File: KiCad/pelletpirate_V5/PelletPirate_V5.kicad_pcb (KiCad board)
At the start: 2 copper layers, 65 x 110 mm, 105 parts, among them J1 SJ1-3523NG_Jack_PP, J2 SJ1-3523NG_Jack_PP, J3 SJ1-3523NG_Jack_PP, J4 SJ1-3523NG_Jack_PP, J5 SJ1-3523NG_Jack_PP, J6 Conn_01x04, T1 BTA12-Triac, T2 BTA12-Triac, T3 BTA12-Triac

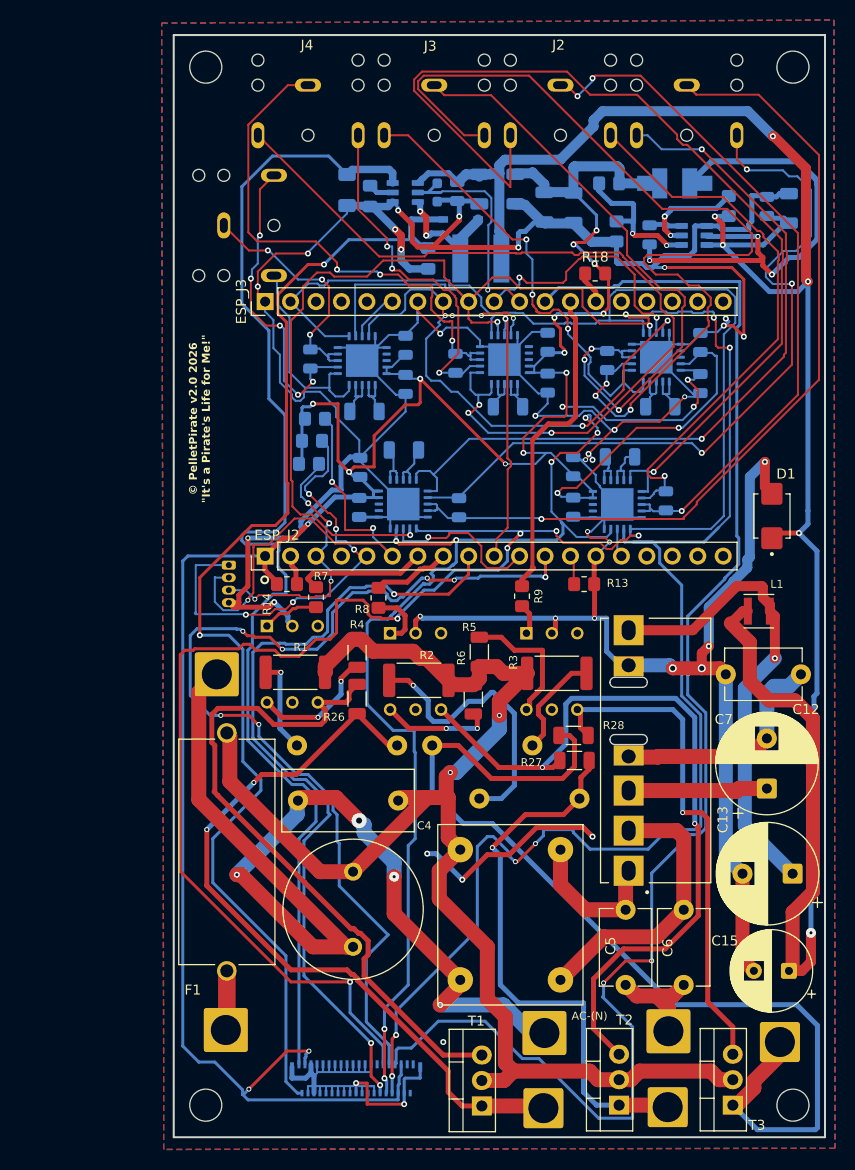
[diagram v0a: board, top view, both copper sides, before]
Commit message: V5 Phase B/C checkpoint: Update-PCB applied, placement in progress
Board now carries the full V5 netlist: S3/USB/ZC/hopper/switch/LED
footprints on board, SDO net renamed to ALL_SDO across existing copper
(tracks preserved), fan channel = MOC3053M with verified Panasonic
ERJ-UP6F1800V drive resistors, DNP flags cleared, WirePad5 relinked.
New parts rough-placed; nets locked next, then arrangement and routing.
FPC1 decision: moving to top-left (side B) pending flex-reach check.

Hard-won process lessons this session: Update-PCB must run with
re-link-by-reference CHECKED (UUID matching deletes re-associated
footprints); preview dialogs can serve stale reports — regenerate
fresh after schematic saves; editor memory can diverge from disk after
undo chains — verify against the file and close-without-save to recover.

Co-Authored-By: Claude Fable 5 <noreply@anthropic.com>
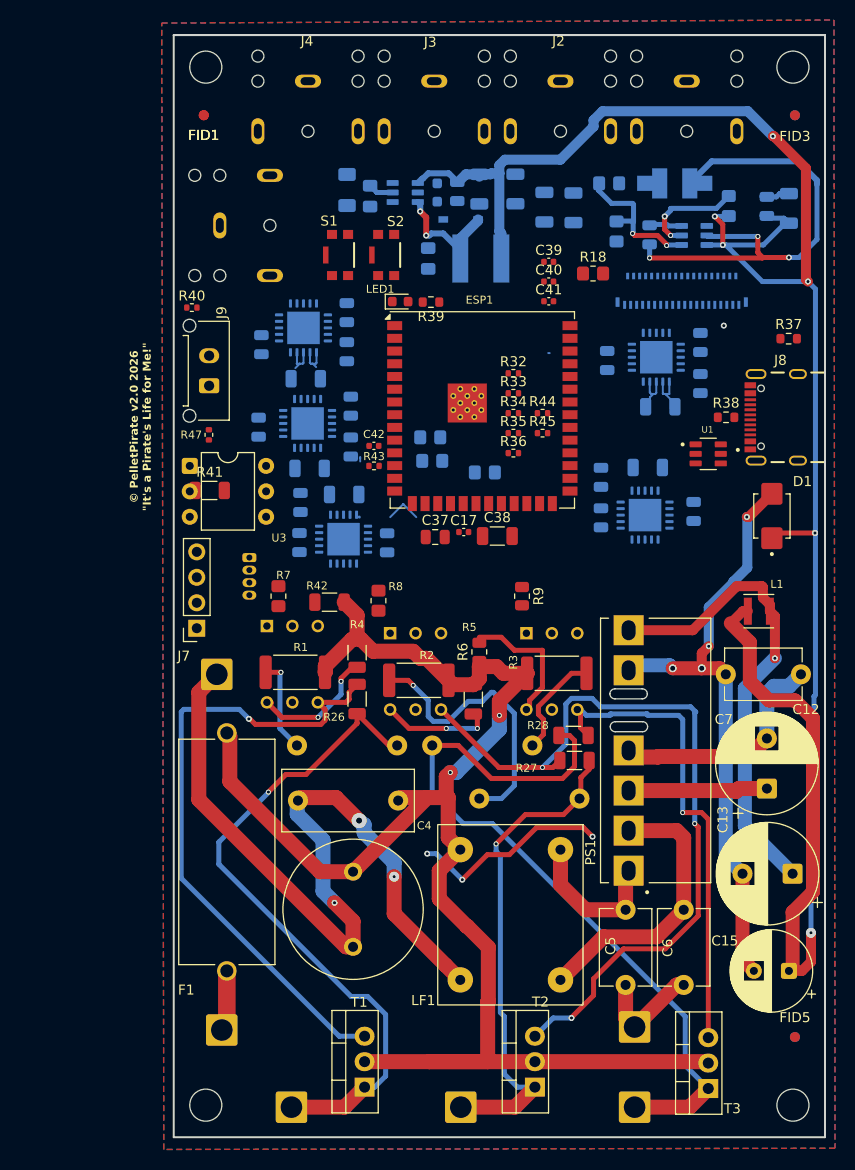
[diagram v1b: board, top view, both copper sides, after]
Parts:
- removed AC-(N): AC-NEUTRAL, Connector_Wire:SolderWire-2.5sqmm_1x01_D2.4mm_OD4.4mm
- removed ESP_J2: PelletPirate_J2_01toJ2_19, ESP32-Footprint-PelletPirate-02x19x2=39:PinHeader_J2x19_P2.54mm_Vertical_PelletPirate
- removed ESP_J3: PelletPirate_J3_01toJ3_19, ESP32-Footprint-PelletPirate-02x19x2=39:PinHeader_J3x19_P2.54mm_Vertical_PelletPirate
- removed R13, R14: 10KΩ, Resistor_SMD:R_0805_2012Metric_Pad1.20x1.40mm_HandSolder
- added C17: 0.1µF 25V, Capacitor_SMD:C_0402_1005Metric, F.Cu at (148.9, 89.6)
- added C37: 1µF 25V, Capacitor_SMD:C_0805_2012Metric, F.Cu at (146.1, 90.1)
- added C38: 10µF 25V, Capacitor_SMD:C_1206_3216Metric, F.Cu at (152.3, 90.0)
- added C39: 0.1µF 25V, Capacitor_SMD:C_0402_1005Metric, F.Cu at (157.4, 62.6)
- added C40: 0.1µF 25V, Capacitor_SMD:C_0402_1005Metric, F.Cu at (157.4, 64.6)
- added C41: 0.1µF 25V, Capacitor_SMD:C_0402_1005Metric, F.Cu at (157.4, 66.6)
- added C42: 1000pF 50V, Capacitor_SMD:C_0402_1005Metric, F.Cu at (140.0, 81.0)
- added ESP1: ESP32-S3-WROOM-1U-N16R8-flyman, Expressif_S3_N16R8_Chip_N1U:ESP32-S3-WROOM-1U-flyman, F.Cu at (150.8, 77.4)
- added FID1 (x2): Fiducial_1mm_Mask2mm, Fiducial:Fiducial_1mm_Mask2mm, F.Cu at (123.0, 48.0)
- added FID3: Fiducial_1mm_Mask2mm, Fiducial:Fiducial_1mm_Mask2mm, F.Cu at (182.0, 48.0)
- added FID4: Fiducial_1mm_Mask2mm, Fiducial:Fiducial_1mm_Mask2mm, B.Cu at (182.0, 48.0)
- added FID5: Fiducial_1mm_Mask2mm, Fiducial:Fiducial_1mm_Mask2mm, F.Cu at (182.0, 140.0)
- added FID6: Fiducial_1mm_Mask2mm, Fiducial:Fiducial_1mm_Mask2mm, B.Cu at (182.0, 140.0)
- added J7: Conn_01x04_Socket, Connector_PinSocket_2.54mm:PinSocket_1x04_P2.54mm_Vertical, F.Cu at (122.3, 99.2)
- added J8: USB4105-GF-A_fly, USB_try2:GCT_USB4105-GF-A_flyman, F.Cu at (182.3, 78.2)
- added J9: Conn_01x02, Connector_Molex:Molex_Micro-Fit_3.0_43650-0215_1x02_P3.00mm_Vertical, F.Cu at (123.5, 75.0)
- added LED1: LTST-C191KGKT_flyman, LED_SMD:LED_0603_1608Metric, F.Cu at (142.6, 66.6)
- added R32: 10KΩ, Resistor_SMD:R_0402_1005Metric, F.Cu at (153.9, 73.8)
- added R33: 10KΩ, Resistor_SMD:R_0402_1005Metric, F.Cu at (153.9, 75.8)
- added R34: 10KΩ, Resistor_SMD:R_0402_1005Metric, F.Cu at (153.9, 77.7)
- added R35: 10KΩ, Resistor_SMD:R_0402_1005Metric, F.Cu at (153.9, 79.7)
- added R36: 10KΩ, Resistor_SMD:R_0402_1005Metric, F.Cu at (153.9, 81.7)
- added R37: 5.1KΩ, Resistor_SMD:R_0603_1608Metric, F.Cu at (181.4, 70.3)
- added R38: 5.1KΩ, Resistor_SMD:R_0603_1608Metric, F.Cu at (175.1, 78.2)
- added R39: 1KΩ, Resistor_SMD:R_0603_1608Metric, F.Cu at (145.7, 66.7)
- added R40: 10KΩ, Resistor_SMD:R_0402_1005Metric, F.Cu at (121.8, 67.2)
- added R41: 15KΩ, Resistor_SMD:R_1206_3216Metric, F.Cu at (123.6, 85.5)
- added R42: 15KΩ, Resistor_SMD:R_1206_3216Metric, F.Cu at (135.6, 96.6)
- added R43: 10KΩ, Resistor_SMD:R_0402_1005Metric, F.Cu at (140.0, 83.0)
- added R44: 10KΩ, Resistor_SMD:R_0402_1005Metric, F.Cu at (156.8, 77.7)
- added R45: 10KΩ, Resistor_SMD:R_0402_1005Metric, F.Cu at (156.8, 79.7)
- added R47: 100Ω, Resistor_SMD:R_0402_1005Metric, F.Cu at (123.5, 79.9)
- added S1: KMR221GLFS, KMR221GLFS_SMD_boot_reset_switch:SW_KMR221GLFS, F.Cu at (136.6, 62.0)
- added S2: KMR221GLFS, KMR221GLFS_SMD_boot_reset_switch:SW_KMR221GLFS, F.Cu at (141.2, 62.0)
- added U1: USBLC6-2SC6, USBC6-2SC6:SOT95P280X145-6N, F.Cu at (173.3, 81.8)
- added U3: H11AA1M, Package_DIP:DIP-6_W7.62mm, F.Cu at (121.6, 83.0)
- Earth1, WirePad1, WirePad2: footprint Connector_Wire:SolderWire-2.5sqmm_1x01_D2.4mm_OD4.4mm -> Connector_Wire:SolderWire-1.5sqmm_1x01_D1.7mm_OD3mm
- MOC3: value MOC3063M -> MOC3053M; footprint MOC3063M-PP2:MOC3063M-PP2 -> MOC3053M_Opto_FanPulse:DIP762W46P254L851H508Q6
- PS1: footprint PBO-5F-12_PP_Try2:PBO-5F-12_pp2 -> NewPBO-5F-12-try:CONV_PBO-5F-12_AUDIT_FLYMAN
- R6: value 360Ω 1/4W -> 180Ω; footprint Resistor_SMD:R_1206_3216Metric -> Resistor_SMD:R_0805_2012Metric
- R9: value 330Ω -> 180Ω; footprint Resistor_SMD:R_0805_2012Metric_Pad1.20x1.40mm_HandSolder -> Resistor_SMD:R_0805_2012Metric
- T3: value BTA12-Triac -> BTA12-600BWRG
- WirePad3, WirePad4, WirePad5: footprint Connector_Wire:SolderWire-2.5sqmm_1x01_D2.4mm_OD3.6mm -> Connector_Wire:SolderWire-1.5sqmm_1x01_D1.7mm_OD3mm
- moved FPC1 85.1 mm to (170.7, 65.5), turned to 180 degrees
- moved WirePad3 25.2 mm to (131.8, 147.0)
- moved R24 20.7 mm to (133.6, 83.3)
- moved C29 20.7 mm to (128.5, 79.1)
- moved C24 20.7 mm to (137.7, 77.0)
- moved C34 20.7 mm to (137.7, 81.1)
- moved MAX4 20.7 mm to (133.4, 78.8)
- moved WirePad4 20.7 mm to (148.7, 147.0)
- moved R31 17.8 mm to (151.1, 83.7)
- moved WirePad5 15.9 mm to (166.0, 147.0)
- moved R29 12.4 mm to (145.6, 80.2)
- moved R30 12.2 mm to (145.8, 82.5)
- moved T1 11.9 mm to (139.1, 145.0)
- moved T2 8.59 mm to (156.1, 145.0)
- moved C26 7.98 mm to (141.3, 90.7)
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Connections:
- net /MAX_SDO renamed /ALL_SDO
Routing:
- net GND: track 490.4 -> 89.0 mm, vias 35 -> 8
- net +3.3V: track 299.7 -> 0.14 mm, vias 20 -> 0
- net /ALL_SCLK: track 239.1 -> 0.00 mm, vias 10 -> 0
- net /ALL_SDI: track 222.0 -> 0.00 mm, vias 6 -> 0
- net /ALL_SDO: track 169.5 -> 0.00 mm, vias 13 -> 0
- net /LCD_RST: track 144.7 -> 0.00 mm, vias 2 -> 0
- net /LED-: track 121.8 -> 0.00 mm
- net /LED+: track 120.5 -> 0.00 mm, vias 2 -> 0
- net /LCD_DC: track 100.1 -> 0.00 mm, vias 7 -> 0
- net Net-(J2-Ring): track 98.7 -> 0.00 mm, vias 1 -> 0
- net Net-(J3-Tip): track 95.7 -> 0.00 mm, vias 3 -> 0
- net Net-(J4-Ring): track 86.6 -> 0.00 mm, vias 3 -> 0
- net Net-(J1-Sleeve): track 85.7 -> 0.00 mm, vias 1 -> 0
- net /LCD_CS: track 80.7 -> 0.00 mm, vias 3 -> 0
- net Net-(J1-Ring): track 76.6 -> 0.02 mm, vias 2 -> 0
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
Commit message: V5: net classes + custom DRC rules live; routing underway
Ported V4's 15 net classes with all five dead patterns FIXED (ALL_SCLK,
ALL_SDO, U3-IN2, PS1-+VO, ESP1-* — were silently unmatched typos in V4)
plus new memberships for the snubber midpoints. Created
PelletPirate_V5.kicad_dru: V4's 7 rules incl. the 2.5mm mains-SELV
barrier (values verified against the 2026-07-28 fab archive), with the
U3-IN2 name-crutch clauses removed per the file's own TODO. Netclass-
width routing confirmed working. AC-side placement done; U3 on the
isolation boundary, ZC RC parts near ESP1.

Co-Authored-By: Claude Fable 5 <noreply@anthropic.com>
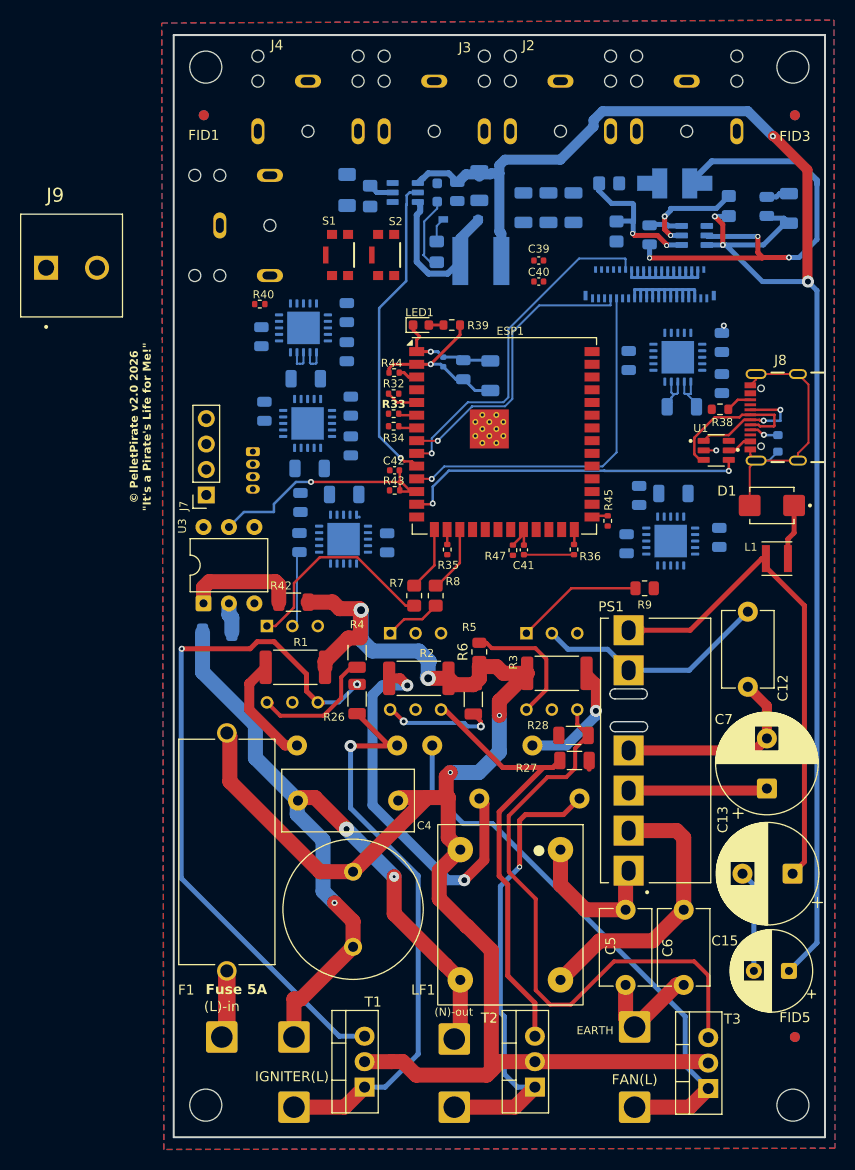
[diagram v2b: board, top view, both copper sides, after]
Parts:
- removed R18, R29, R30, R31: 10KΩ, Resistor_SMD:R_0805_2012Metric_Pad1.20x1.40mm_HandSolder
- added WirePad6: (N)-out, Connector_Wire:SolderWire-1.5sqmm_1x01_D1.7mm_OD3mm, F.Cu at (148.0, 140.2)
- C17, C37, C38, R37, R41: moved to B.Cu
- F1: value Fuse 2A -> Fuse 5A
- FID2: renamed from FID1; moved to B.Cu
- J9: value Conn_01x02 -> TB007-508-02BE; footprint Connector_Molex:Molex_Micro-Fit_3.0_43650-0215_1x02_P3.00mm_Vertical -> SameSky_Screw_Terminal:CUI_TB007-508-02BE
- WirePad1: value LOAD-In -> (L)-in
- moved WirePad2 37.0 mm to (132.0, 140.0)
- moved R47 32.4 mm to (153.8, 91.4)
- moved C41 24.9 mm to (154.9, 91.4), turned to 90 degrees
- moved J9 20.1 mm to (107.3, 63.2), turned to 0 degrees
- moved C17 17.1 mm to (146.9, 72.6), turned to 90 degrees
- moved C37 16.9 mm to (148.9, 73.4), turned to 90 degrees
- moved C38 16.0 mm to (151.6, 74.0), turned to 90 degrees
- moved R44 15.4 mm to (142.0, 73.7), turned to 180 degrees
- moved R41 14.2 mm to (124.3, 99.6)
- moved U3 13.8 mm to (123.0, 96.7), turned to 90 degrees
- moved R7 13.6 mm to (144.0, 96.0)
- moved R35 13.4 mm to (147.3, 91.3), turned to -90 degrees
- moved J7 13.3 mm to (123.2, 85.9)
- moved R9 12.3 mm to (167.0, 95.2), turned to 180 degrees
- moved R33 12.1 mm to (141.9, 77.8), turned to 180 degrees
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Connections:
- J9 pad 1: Net-(J9-Pin_1) -> Net-(J9-Pad1)
- R40 pad 2: Net-(J9-Pin_1) -> Net-(J9-Pad1)
- R47 pad 1: Net-(ESP1-IO14) -> Net-(J9-Pad1)
- R47 pad 2: Net-(J9-Pin_1) -> Net-(ESP1-IO14)
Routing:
- net +12V: track 211.6 -> 169.2 mm, vias 6 -> 4
- net GND: track 89.0 -> 128.8 mm, vias 8 -> 3
- net /LCD_DC: track 0.00 -> 36.4 mm, vias 0 -> 1
- net /LCD_CS: track 0.00 -> 34.8 mm, vias 0 -> 1
- net /USB_D-: track 0.00 -> 34.6 mm, vias 0 -> 2
- net Net-(T2-G): track 78.4 -> 45.6 mm, vias 3 -> 0
- net /LED_PWM: track 0.00 -> 31.4 mm, vias 0 -> 1
- net /LCD_RST: track 0.00 -> 29.6 mm, vias 0 -> 1
- net /ZC_DET: track 0.00 -> 25.2 mm, vias 0 -> 1
- net Net-(MOC1-Pad1): track 0.00 -> 21.0 mm
- net Net-(T3-A1): track 75.9 -> 55.5 mm
- net +3.3V: track 0.14 -> 16.9 mm, vias 0 -> 1
- net /USB-C_D-: track 0.00 -> 15.3 mm
- net Net-(MOC3-Pad1): track 0.00 -> 12.7 mm
- net Net-(T3-G): track 47.6 -> 60.3 mm, vias 1 -> 0
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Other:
- board text added: "3053"

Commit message: V5: connector swaps + MAX CS remap; routing in progress
J8 -> GCT USB4145-03-0070-C vertical USB-C (VBUS_A/B and split data
pins tied per Type-C practice); J9 -> Same Sky TB002-500-02BE 5.00mm
screw terminal (TB007 files replaced with correct TB002 set). MAX CS
lines re-pinned for routing reach: MAX3_CS -> module pad 35 (IO42),
MAX1_CS on a new IO, MAX2/4/5 shuffled among the existing CS GPIOs —
final CS-to-jack map to be extracted from netlist at audit and carried
into boardpins.h as the V5 target delta. 94 DRC violations remain to
triage.

Co-Authored-By: Claude Fable 5 <noreply@anthropic.com>
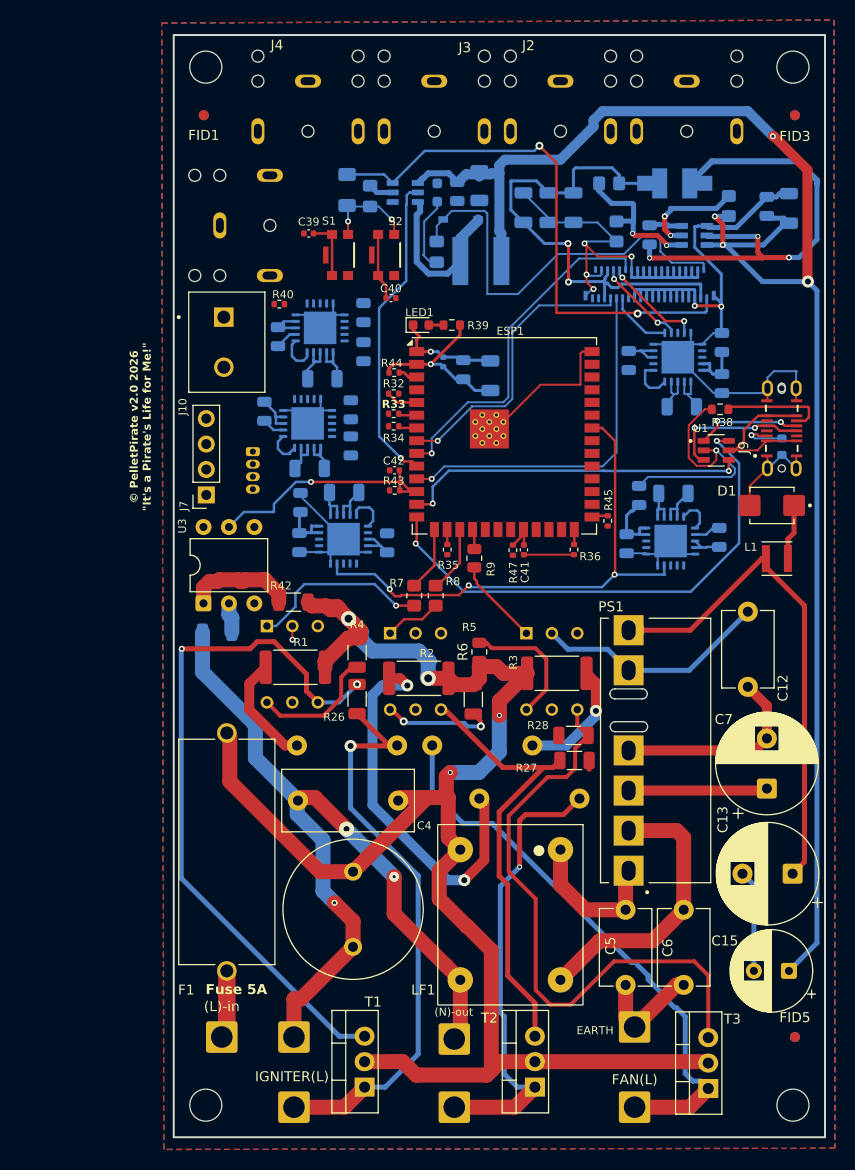
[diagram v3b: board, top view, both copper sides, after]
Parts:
- removed J8: USB4105-GF-A_fly, USB_try2:GCT_USB4105-GF-A_flyman
- added J10: TB002-500-02BE, SameSky_Screw_Terminal:CUI_TB002-500-02BE, F.Cu at (125.0, 68.2)
- J9: value TB007-508-02BE -> USB4145-03-0070-C_REVA2; footprint SameSky_Screw_Terminal:CUI_TB007-508-02BE -> USB_try2:GCT_USB4145-03-0070-C_REVA2
- moved J9 75.1 mm to (180.7, 79.2), turned to 90 degrees
- moved C39 23.1 mm to (133.5, 59.8)
- moved R9 17.3 mm to (150.0, 92.2), turned to -90 degrees
- moved C40 14.8 mm to (141.7, 66.2)
- moved R40 1.95 mm to (130.5, 66.8)
- moved MAX5 1.66 mm to (134.6, 69.2)
- moved C25 1.66 mm to (138.9, 67.7)
- moved C30 1.66 mm to (130.4, 70.1)
- moved C35 1.66 mm to (138.9, 71.6)
- moved R25 1.66 mm to (134.8, 74.3)
- moved R37 0.52 mm to (180.7, 81.1)
- moved C24 0.37 mm to (137.7, 77.4)
- moved R21 0.20 mm to (137.0, 85.7)
- turned C20 to 90 degrees
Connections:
- ESP1 pad 20: /MAX2_CS -> /MAX4_CS
- ESP1 pad 23: /MAX3_CS -> /MAX1_CS
- ESP1 pad 24: /MAX4_CS -> unconnected-(ESP1-IO47-Pad24)
- ESP1 pad 25: /MAX5_CS -> /MAX2_CS
- ESP1 pad 35: unconnected-(ESP1-IO42-Pad35) -> /MAX3_CS
- ESP1 pad 4: /MAX1_CS -> /MAX5_CS
- R37 pad 1: Net-(J8-CC1) -> Net-(J9-CC1)
- R38 pad 1: Net-(J8-CC2) -> Net-(J9-CC2)
- R40 pad 2: Net-(J9-Pad1) -> Net-(J10-Pad1)
- R47 pad 1: Net-(J9-Pad1) -> Net-(J10-Pad1)
- U1 pad 5: VBUS -> VBUS_A
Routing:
- net GND: track 128.8 -> 274.3 mm, vias 3 -> 11
- net +3.3V: track 16.9 -> 85.7 mm, vias 1 -> 3
- net /ALL_SDO: track 0.00 -> 63.1 mm, vias 0 -> 5
- net /LED-: track 0.00 -> 54.9 mm, vias 0 -> 2
- net /USB_D+: track 0.00 -> 51.3 mm, vias 0 -> 2
- net /LED+: track 2.47 -> 41.8 mm
- net VBUS_A: track 0.00 -> 16.0 mm
- net Net-(J9-CC2): track 0.00 -> 10.5 mm
- net /ALL_SCLK: track 0.00 -> 9.11 mm, vias 0 -> 2
- net Net-(ESP1-IO0): track 1.61 -> 8.30 mm
- net /ALL_SDI: track 0.00 -> 6.29 mm
- net Net-(ESP1-EN): track 1.92 -> 7.91 mm
- net Net-(J9-CC1): track 0.00 -> 4.80 mm, vias 0 -> 1
- net Net-(J1-Sleeve): track 0.00 -> 4.64 mm
- net Net-(J3-Ring): track 0.00 -> 4.52 mm
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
